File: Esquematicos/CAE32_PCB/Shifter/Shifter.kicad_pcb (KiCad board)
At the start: 4 copper layers, 48.9 x 42.6 mm, 42 parts, among them J1 EXP-PORT, J2 SPI_DEVICE, J3 Conn_01x08_Female, J4 Conn_01x08_Female, J5 Conn_01x08_Female, J6 USB_C_Receptacle_USB2.0, SW1 USB_BOOT, U1 RP2040, U2 W25Q16JVSNIQ, U3 AP2112K-3.3, U4 USBLC6-2P6, Y1 12Mhz

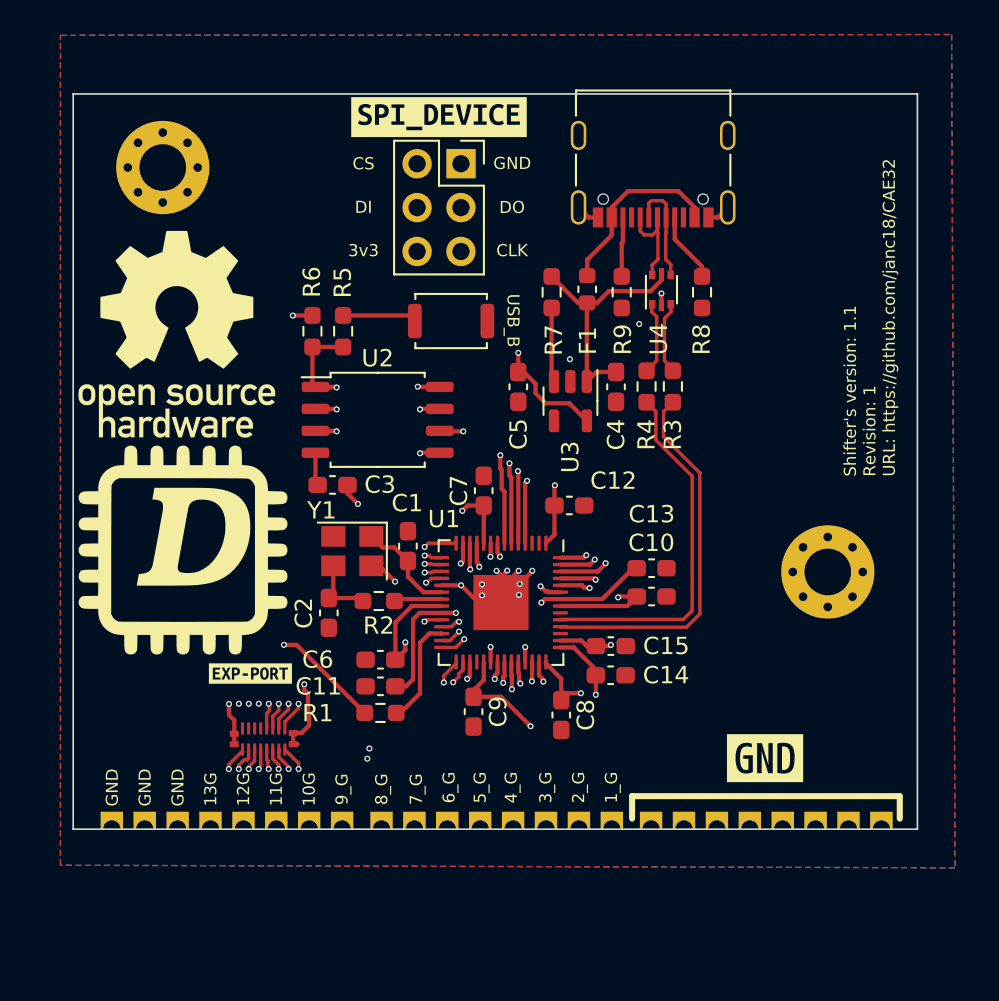
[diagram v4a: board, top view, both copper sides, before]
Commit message: update: changed the castelled holes for pin sockets and changed 0603 footprints to 0402
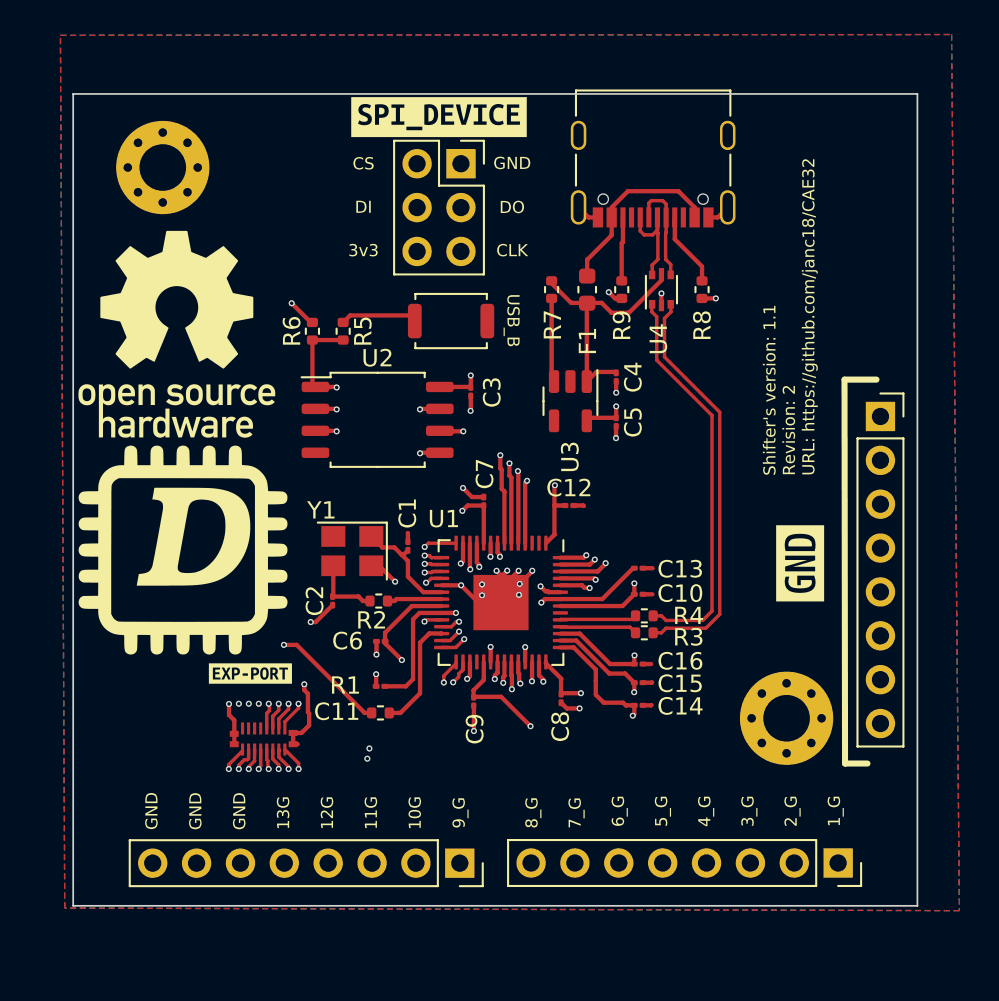
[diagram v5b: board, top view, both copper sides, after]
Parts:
- added C16: 1u, Capacitor_SMD:C_01005_0402Metric, F.Cu at (176.6, 106.8)
- C1, C10, C11, C12, C13, C14, C15, C2, C3, C4, C5, C6, C7, C8, C9: footprint Capacitor_SMD:C_0603_1608Metric_Pad1.08x0.95mm_HandSolder -> Capacitor_SMD:C_01005_0402Metric
- J3, J4, J5: footprint shifter:shi -> Connector_PinSocket_2.54mm:PinSocket_1x08_P2.54mm_Vertical
- R1, R2, R3, R4, R5, R6, R7, R8, R9: footprint Resistor_SMD:R_0603_1608Metric_Pad0.98x0.95mm_HandSolder -> Resistor_SMD:R_0402_1005Metric
- moved J5 25.1 mm to (190.6, 92.4), turned to 0 degrees
- moved J3 20.8 mm to (188.1, 118.3)
- moved J4 14.6 mm to (166.2, 118.3)
- moved R3 14.4 mm to (176.9, 104.9), turned to 0 degrees
- moved R4 13.3 mm to (176.9, 104.0), turned to 0 degrees
- moved kibuzzard-64F4C3CA 11.5 mm to (185.9, 100.9), turned to 90 degrees
- moved C3 9.65 mm to (166.9, 91.0), turned to -90 degrees
- moved H2 8.80 mm to (185.1, 109.9)
- moved C5 6.03 mm to (175.3, 92.7)
- moved C15 2.66 mm to (176.6, 107.8)
- moved C14 2.38 mm to (176.6, 109.1)
- moved C6 1.06 mm to (161.7, 105.4)
- moved C8 0.96 mm to (172.1, 108.7)
- moved C10 0.76 mm to (176.6, 102.7)
- moved C13 0.75 mm to (176.6, 101.2)
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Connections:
- net /Power/VBUS renamed VBUS
- U1 pad 45: unconnected-(U1-VREG_VOUT-Pad45) -> +3V3
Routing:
- net /Power/D-: track 4.27 -> 23.7 mm
- net /Power/D+: track 4.23 -> 23.0 mm
- net /D-: track 21.8 -> 4.50 mm
- net /D+: track 21.0 -> 4.45 mm
- net GNDREF: track 22.5 -> 35.1 mm, vias 17 -> 26
- net /1_GEAR: track 11.4 -> 23.7 mm
- net /2_GEAR: track 10.8 -> 22.8 mm
- net /3_GEAR: track 14.4 -> 25.2 mm
- net /4_GEAR: track 10.7 -> 19.6 mm
- net +3V3: track 64.0 -> 71.5 mm
- net /10_GEAR: track 40.2 -> 47.5 mm
- net /11_GEAR: track 40.6 -> 47.8 mm
- net /9_GEAR: track 38.7 -> 45.6 mm
- net /12_GEAR: track 37.5 -> 43.7 mm
- net /5_GEAR: track 10.4 -> 16.0 mm
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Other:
- board size 48.9 x 42.6 mm -> 48.9 x 47 mm
- board text added: "Shifter's version: 1.1 Revision: 2 URL: https://github.com/janc18/CAE32"
- board text removed: "Shifter's version: 1.1 Revision: 1 URL: https://github.com/janc18/CAE32"

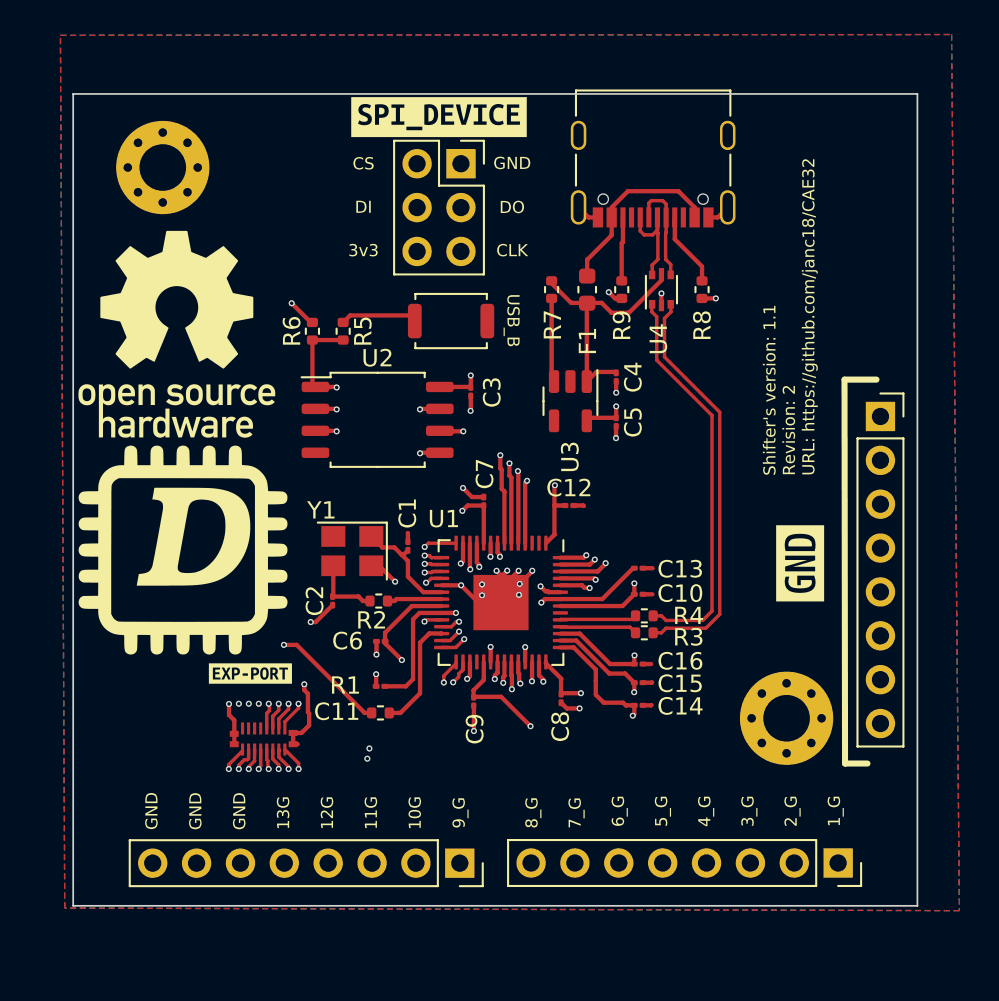
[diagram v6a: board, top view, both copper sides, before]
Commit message: update: added minor improvements to Shifter's PCB
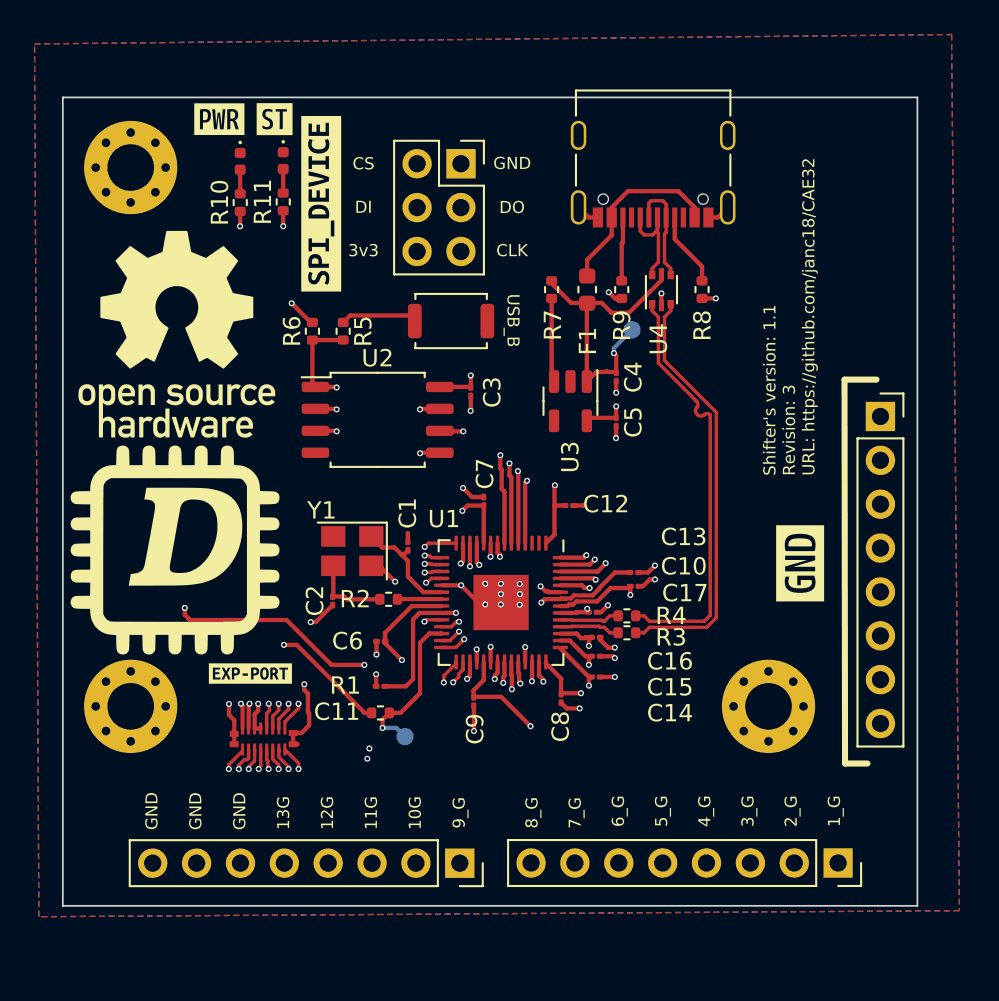
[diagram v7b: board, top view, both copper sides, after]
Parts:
- added C17: 0u1, Capacitor_SMD:C_01005_0402Metric, F.Cu at (173.9, 103.8)
- added D1: PWR, LED_SMD:LED_0402_1005Metric, F.Cu at (153.5, 77.6)
- added D2: STATUS, LED_SMD:LED_0402_1005Metric, F.Cu at (156.0, 77.6)
- added H3: MH, MountingHole:MountingHole_2.7mm_M2.5_Pad_Via, F.Cu at (147.2, 109.2)
- added R10: 27, Resistor_SMD:R_0402_1005Metric, F.Cu at (153.5, 80.0)
- added R11: 27, Resistor_SMD:R_0402_1005Metric, F.Cu at (156.0, 80.0)
- added TP1: RS, TestPoint:TestPoint_Pad_D1.0mm, B.Cu at (163.1, 111.0)
- added TP2: 5v, TestPoint:TestPoint_Pad_D1.0mm, B.Cu at (176.2, 87.4)
- added kibuzzard-6511E845: G***, kibuzzard-6511E845, F.Cu at (152.3, 75.2)
- added kibuzzard-6511E886: G***, kibuzzard-6511E886, F.Cu at (155.5, 75.2)
- added kibuzzard-651234A4: G***, kibuzzard-651234A4, B.Cu at (178.3, 87.4)
- added kibuzzard-651234C4: G***, kibuzzard-651234C4, B.Cu at (163.1, 113.0)
- H1, H2: value MountingHole -> MH
- R6: value 10k -> DNF
- moved kibuzzard-64B759C0 8.47 mm to (158.2, 80.1), turned to 90 degrees
- moved C14 2.97 mm to (174.1, 107.5)
- moved C16 2.92 mm to (174.1, 105.2)
- moved C15 2.91 mm to (174.1, 106.3)
- moved H1 1.86 mm to (147.2, 78.0)
- moved H2 1.25 mm to (184.1, 109.2)
- moved R3 1.01 mm to (175.9, 104.9)
- moved R4 1.01 mm to (175.9, 104.0)
- moved R2 0.58 mm to (162.1, 103.0)
- moved C10 0.51 mm to (176.3, 102.2)
- moved C13 0.36 mm to (176.3, 101.5)
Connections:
- J1 pad 10: unconnected-(J1-Pin_10-Pad10) -> +3V3
- J1 pad 11: unconnected-(J1-Pin_11-Pad11) -> +3V3
- J1 pad 12: unconnected-(J1-Pin_12-Pad12) -> +3V3
- J1 pad 9: unconnected-(J1-Pin_9-Pad9) -> +3V3
- U1 pad 32: unconnected-(U1-GPIO21-Pad32) -> /STATUS
- U1 pad 48: unconnected-(U1-USB_VDD-Pad48) -> +3V3
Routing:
- net /STATUS: track 0.00 -> 45.2 mm, vias 0 -> 4
- net GNDREF: track 35.1 -> 31.1 mm, vias 26 -> 29
- net +3V3: track 71.5 -> 68.2 mm, vias 14 -> 19
- net +5V: track 14.7 -> 17.7 mm, vias 0 -> 1
- net /RESET: track 6.66 -> 9.21 mm, vias 0 -> 1
- net /Power/D+: track 23.0 -> 24.6 mm
- net Net-(D2-A): track 0.00 -> 1.40 mm
- net Net-(D1-A): track 0.00 -> 1.39 mm
- net /D-: track 4.50 -> 3.51 mm
- net /D+: track 4.45 -> 3.51 mm
- net /Power/D-: track 23.7 -> 24.6 mm
- net /XOUT: track 3.18 -> 2.57 mm
- net Net-(C2-Pad1): track 3.88 -> 4.40 mm
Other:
- board size 48.9 x 47 mm -> 49.5 x 46.8 mm
- board text added: "Shifter's version: 1.1 Revision: 3 URL: https://github.com/janc18/CAE32"
- board text removed: "Shifter's version: 1.1 Revision: 2 URL: https://github.com/janc18/CAE32"

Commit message: update: redesign of the shifter PCB, changing the PCB requirements(via from 0.15 to 0.3mm) and pin sockets for FCP connectors
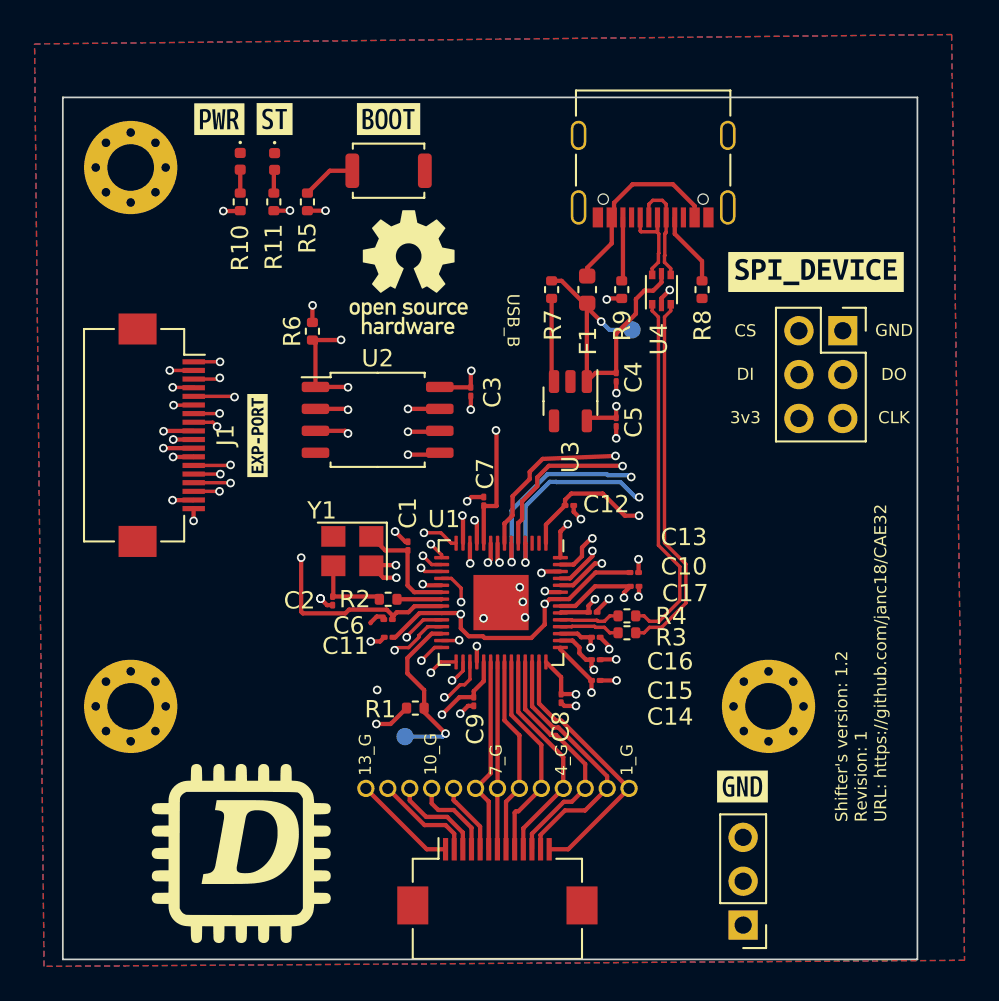
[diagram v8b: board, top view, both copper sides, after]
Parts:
- removed kibuzzard-64F4C3CA: G***, kibuzzard-64F4C3CA
- added kibuzzard-6517AD32: G***, kibuzzard-6517AD32, F.Cu at (162.1, 75.2)
- added kibuzzard-6518B6F6: G***, kibuzzard-6518B6F6, F.Cu at (182.6, 113.8)
- J1: footprint shifter:BM28B0-6-16DS -> Connector_FFC-FPC:Hirose_FH12-18S-0.5SH_1x18-1MP_P0.50mm_Horizontal
- J3: value Conn_01x08_Female -> Conn_01x13_Socket; footprint Connector_PinSocket_2.54mm:PinSocket_1x08_P2.54mm_Vertical -> shifter:Pad_1x13_THT_1.27mm
- J4: value Conn_01x08_Female -> Conn_01x13_Socket; footprint Connector_PinSocket_2.54mm:PinSocket_1x08_P2.54mm_Vertical -> Connector_FFC-FPC:Hirose_FH12-13S-0.5SH_1x13-1MP_P0.50mm_Horizontal
- J5: value Conn_01x08_Female -> Conn_01x03_Socket; footprint Connector_PinSocket_2.54mm:PinSocket_1x08_P2.54mm_Vertical -> Connector_PinHeader_2.54mm:PinHeader_1x03_P2.54mm_Vertical
- TP1: value RS -> TP
- TP2: value 5v -> TP
- U2: value W25Q16JVSNIQ -> W25Q128JVS
- moved J5 30.5 mm to (182.6, 121.9), turned to 180 degrees
- moved kibuzzard-64B759C0 28.9 mm to (186.8, 84.0), turned to 0 degrees
- moved J2 24.1 mm to (188.4, 87.5)
- moved J3 20.2 mm to (168.4, 114.0), turned to 180 degrees
- moved J1 18.6 mm to (149.0, 93.5), turned to -90 degrees
- moved kibuzzard-64B75D82 13.8 mm to (154.5, 93.5), turned to 90 degrees
- moved SW1 9.43 mm to (162.1, 78.2)
- moved R5 7.77 mm to (157.4, 80.0)
- moved C11 2.88 mm to (162.1, 105.2)
- moved J4 2.41 mm to (168.4, 119.3), turned to 0 degrees
- moved R1 2.04 mm to (163.7, 109.3)
- moved C6 1.34 mm to (162.1, 104.2)
- moved R11 0.54 mm to (155.5, 80.0)
- moved D2 0.50 mm to (155.5, 77.7)
- moved C14 0.20 mm to (174.1, 107.7)
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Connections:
- J1 pad 1: /GPIO_18 -> /GPIO_11
- J1 pad 13: /SWCLK -> /GPIO_20
- J1 pad 14: /SWDIO -> /GPIO_19
- J1 pad 15: /GPIO_20 -> /GPIO_18
- J1 pad 16: /GPIO_19 -> /GPIO_17
- J1 pad 2: /GPIO_17 -> /GPIO_12
- J1 pad 3: /GPIO_16 -> /GPIO_13
- J1 pad 4: /GPIO_15 -> /GPIO_14
- J1 pad 5: /GPIO_14 -> /GPIO_15
- J1 pad 6: /GPIO_13 -> /GPIO_16
- J1 pad 7: /GPIO_12 -> /SWCLK
- J1 pad 8: /GPIO_11 -> /SWDIO
- J4 pad 1: /9_GEAR -> /13_GEAR
- J4 pad 2: /10_GEAR -> /12_GEAR
- J4 pad 4: /12_GEAR -> /10_GEAR
- J4 pad 5: /13_GEAR -> /9_GEAR
- J4 pad 6: GNDREF -> /8_GEAR
- J4 pad 7: GNDREF -> /7_GEAR
- J4 pad 8: GNDREF -> /6_GEAR
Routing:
- net /10_GEAR: track 47.2 -> 21.7 mm
- net /11_GEAR: track 47.6 -> 24.0 mm
- net /9_GEAR: track 45.6 -> 24.2 mm
- net /GPIO_19: track 14.8 -> 32.5 mm, vias 3 -> 2
- net /GPIO_18: track 15.0 -> 30.2 mm
- net /QSPI_CS: track 25.9 -> 39.2 mm, vias 2 -> 4
- net /STATUS: track 45.2 -> 33.2 mm, vias 4 -> 2
- net /3_GEAR: track 25.2 -> 14.0 mm, vias 1 -> 0
- net /GPIO_16: track 19.6 -> 29.4 mm
- net /SWCLK: track 14.1 -> 23.6 mm
- net /GPIO_15: track 19.1 -> 28.6 mm
- net GNDREF: track 31.1 -> 22.0 mm, vias 29 -> 27
- net /GPIO_20: track 17.2 -> 25.9 mm
- net /SPI_CLK: track 18.8 -> 26.9 mm, vias 1 -> 2
- net /SWDIO: track 15.8 -> 23.9 mm
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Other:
- board size 49.5 x 46.8 mm -> 49.5 x 49.9 mm
- board text added: "10_G"
- board text added: "13_G"
- board text added: "Shifter's version: 1.2 Revision: 1 URL: https://github.com/janc18/CAE32"
- board text removed: "10G"
- board text removed: "11G"
- board text removed: "12G"
- board text removed: "13G"
- board text removed: "2_G"
- board text removed: "3_G"
- board text removed: "5_G"
- board text removed: "6_G"
- board text removed: "8_G"
- board text removed: "9_G"
- board text removed: "Shifter's version: 1.1 Revision: 3 URL: https://github.com/janc18/CAE32"
